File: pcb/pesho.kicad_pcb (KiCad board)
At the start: 2 copper layers, 102.5 x 65 mm, 58 parts, among them IC1 4N25, IC2 4N25, IC3 4N25, IC4 4N25, IC5 4N25, IC6 4N25, P1 Power, P2 Bulkey, P3 Raspberry Pi CONN, P4 Serial, U1 JE-112D, U2 JE-112D, U3 JE-112D

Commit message: added test pcb segment
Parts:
- moved C10 142.8 mm to (238.8, 77.8)
- moved C11 142.8 mm to (238.8, 80.3)
- moved C13 142.8 mm to (238.8, 85.3)
- moved C15 142.8 mm to (238.8, 90.3)
- moved C16 142.8 mm to (238.8, 92.8)
- moved C3 142.8 mm to (238.8, 60.3)
- moved C4 142.8 mm to (238.8, 62.8)
- moved C5 142.8 mm to (238.8, 65.3)
- moved C6 142.8 mm to (238.8, 67.8)
- moved C7 142.8 mm to (238.8, 70.3)
- moved C9 142.8 mm to (238.8, 75.3)
- moved R4 142.8 mm to (244.8, 85.3)
- moved R5 142.8 mm to (244.8, 82.8)
- moved R6 142.8 mm to (244.8, 80.3)
- moved D1 82.1 mm to (204.8, 62.8)
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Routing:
- net Net-(D6-Pad1): track 40.4 -> 111.6 mm, vias 0 -> 1
- net Net-(D5-Pad1): track 22.1 -> 87.7 mm, vias 0 -> 1
- net /BLK: track 0.00 -> 43.1 mm
- net /BD: track 0.00 -> 43.0 mm
- net /BUK: track 0.00 -> 41.4 mm
- net +12V: track 257.6 -> 228.9 mm
- net Net-(D4-Pad1): track 45.5 -> 63.1 mm
- net GNDA: track 50.9 -> 57.1 mm, vias 0 -> 1
- net (no net): vias 0 -> 440
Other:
- board size 102.5 x 65 mm -> 102.5 x 95 mm
- board text added: "Initlab Pesho PCB"
- board text added: "rdrlab"

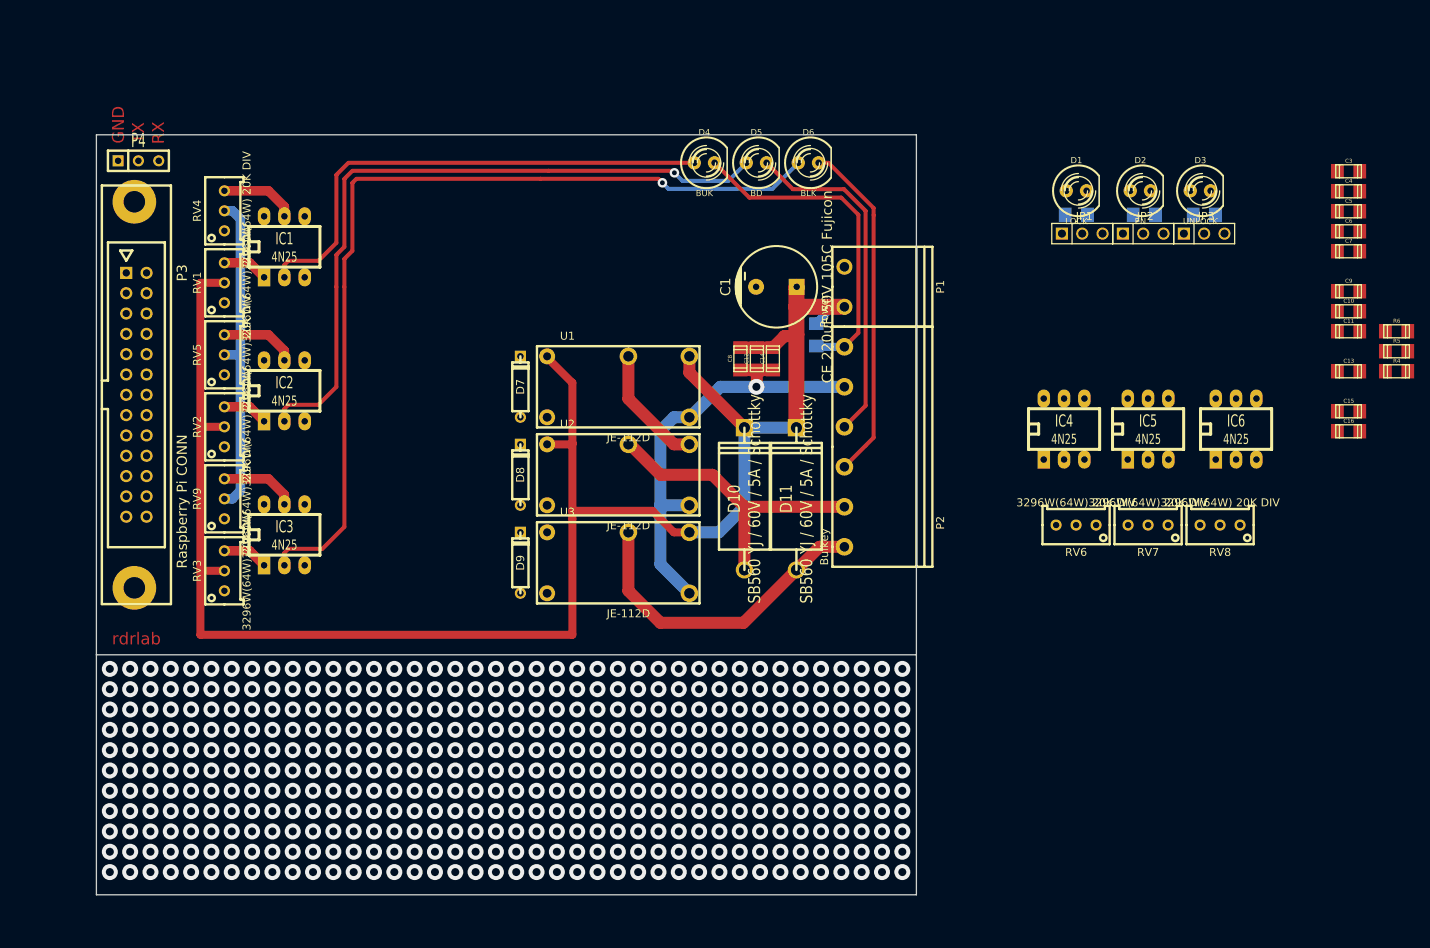
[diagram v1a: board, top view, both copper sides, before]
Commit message: better layout and all components on place
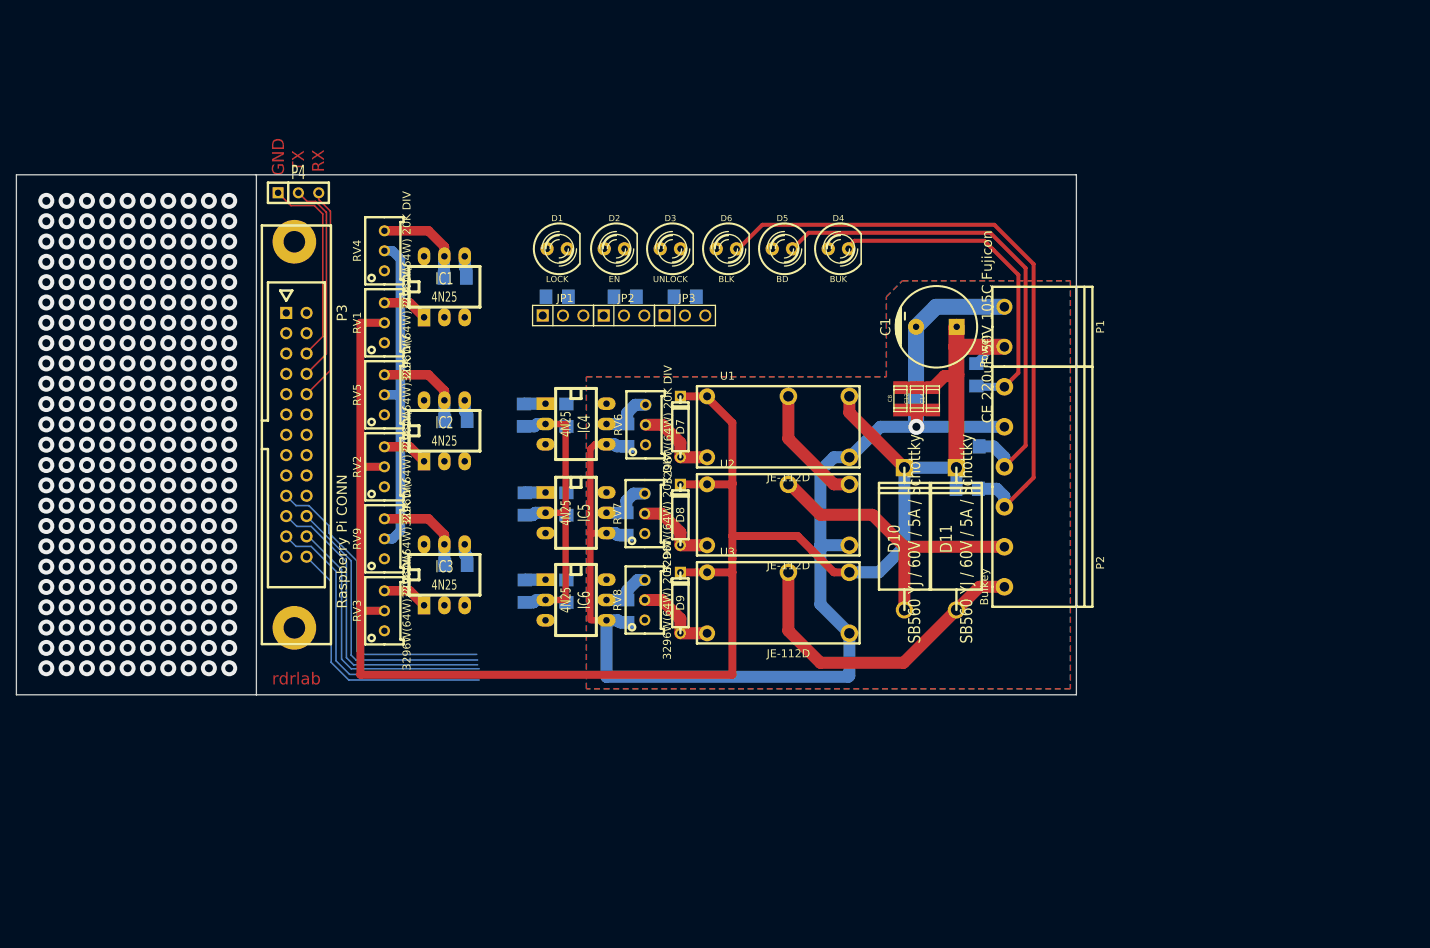
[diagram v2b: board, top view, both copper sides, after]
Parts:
- C10, C11, C13, C15, C16, C3, C4, C5, C6, C7, C9, R4, R5, R6: moved to B.Cu
- moved C16 112.8 mm to (127.2, 109.5), turned to 180 degrees
- moved C13 112.3 mm to (127.1, 73.6), turned to 180 degrees
- moved C15 111.6 mm to (127.2, 91.5), turned to 180 degrees
- moved C7 111.4 mm to (135.8, 112.8), turned to 90 degrees
- moved R6 108.7 mm to (141.0, 112.8), turned to 90 degrees
- moved C6 108.5 mm to (135.8, 101.9), turned to 90 degrees
- moved C5 106.2 mm to (135.7, 90.8), turned to 90 degrees
- moved R5 105.5 mm to (141.0, 101.9), turned to 90 degrees
- moved R4 103.9 mm to (141.0, 90.8), turned to 90 degrees
- moved C11 96.7 mm to (148.6, 115.3), turned to 90 degrees
- moved C10 94.1 mm to (148.5, 104.4), turned to 90 degrees
- moved C9 91.9 mm to (148.6, 93.3), turned to 90 degrees
- moved IC6 85.2 mm to (142.2, 113.9), turned to 270 degrees
- moved RV8 72.5 mm to (150.8, 113.9), turned to 270 degrees
- moved IC5 72.3 mm to (142.2, 103.0), turned to 270 degrees
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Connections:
- C2 pad 2: /BUK -> /BLK
- C4 pad 2: /BLK -> /BUK
- IC1 pad 2: Net-(D4-Pad1) -> Net-(D6-Pad1)
- IC1 pad 6: Net-(IC1-Pad6) -> (no net)
- IC2 pad 6: Net-(IC2-Pad6) -> (no net)
- IC3 pad 2: Net-(D6-Pad1) -> Net-(D4-Pad1)
- IC3 pad 6: Net-(IC3-Pad6) -> (no net)
- IC4 pad 6: Net-(IC4-Pad6) -> (no net)
- IC5 pad 6: Net-(IC5-Pad6) -> (no net)
- IC6 pad 6: Net-(IC6-Pad6) -> (no net)
- P3 pad 11: Net-(P3-Pad11) -> (no net)
- P3 pad 12: Net-(P3-Pad12) -> (no net)
- P3 pad 13: Net-(P3-Pad13) -> (no net)
- P3 pad 15: Net-(P3-Pad15) -> (no net)
- P3 pad 16: Net-(P3-Pad16) -> (no net)
- P3 pad 18: Net-(P3-Pad18) -> (no net)
- P3 pad 2: Net-(P3-Pad2) -> (no net)
- P3 pad 3: Net-(P3-Pad3) -> (no net)
- P3 pad 4: Net-(P3-Pad4) -> (no net)
- P3 pad 5: Net-(P3-Pad5) -> (no net)
- P3 pad 7: Net-(P3-Pad7) -> (no net)
- RV1 pad 3: Net-(RV1-Pad3) -> (no net)
- RV2 pad 3: Net-(RV2-Pad3) -> (no net)
- RV3 pad 3: Net-(RV3-Pad3) -> (no net)
- RV4 pad 3: Net-(RV4-Pad3) -> (no net)
- RV5 pad 3: Net-(RV5-Pad3) -> (no net)
- RV6 pad 3: Net-(RV6-Pad3) -> (no net)
- RV7 pad 3: Net-(RV7-Pad3) -> (no net)
- RV8 pad 3: Net-(RV8-Pad3) -> (no net)
- RV9 pad 3: Net-(RV9-Pad3) -> (no net)
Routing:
- net Net-(D6-Pad1): track 111.6 -> 0.00 mm, vias 1 -> 0
- net GNDA: track 57.1 -> 160.2 mm
- net Net-(D5-Pad1): track 87.7 -> 0.00 mm, vias 1 -> 0
- net GND: track 0.00 -> 71.6 mm
- net Net-(D4-Pad1): track 63.1 -> 0.00 mm
- net /GPIO10: track 0.00 -> 39.2 mm
- net /GPIO9: track 0.00 -> 38.6 mm
- net /GPIO25: track 9.52 -> 48.0 mm
- net /GPIO11: track 0.00 -> 37.8 mm
- net /GPIO8: track 9.52 -> 47.1 mm
- net /GPIO7: track 9.52 -> 46.0 mm
- net /BLK: track 43.1 -> 77.1 mm
- net /RX: track 0.00 -> 27.0 mm
- net /TX: track 0.00 -> 25.7 mm
- net /BD: track 43.0 -> 62.6 mm
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- added copper zone on B.Cu, net GNDA
- added copper zone on F.Cu, net GNDA
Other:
- board size 102.5 x 95 mm -> 132.5 x 65 mm

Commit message: added some traces
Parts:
- R1, R2, R3: moved to F.Cu
- moved R2 1.35 mm to (147.0, 76.0)
- moved R3 1.10 mm to (154.8, 76.0)
- moved R1 0.60 mm to (139.2, 76.0), turned to 0 degrees
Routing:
- net Net-(D4-Pad1): track 0.00 -> 86.2 mm
- net Net-(D5-Pad1): track 0.00 -> 62.1 mm
- net GND: track 71.6 -> 115.2 mm
- net Net-(D6-Pad1): track 0.00 -> 38.4 mm
- net /GPIO25: track 48.0 -> 75.9 mm
- net +3.3V: track 40.8 -> 58.7 mm

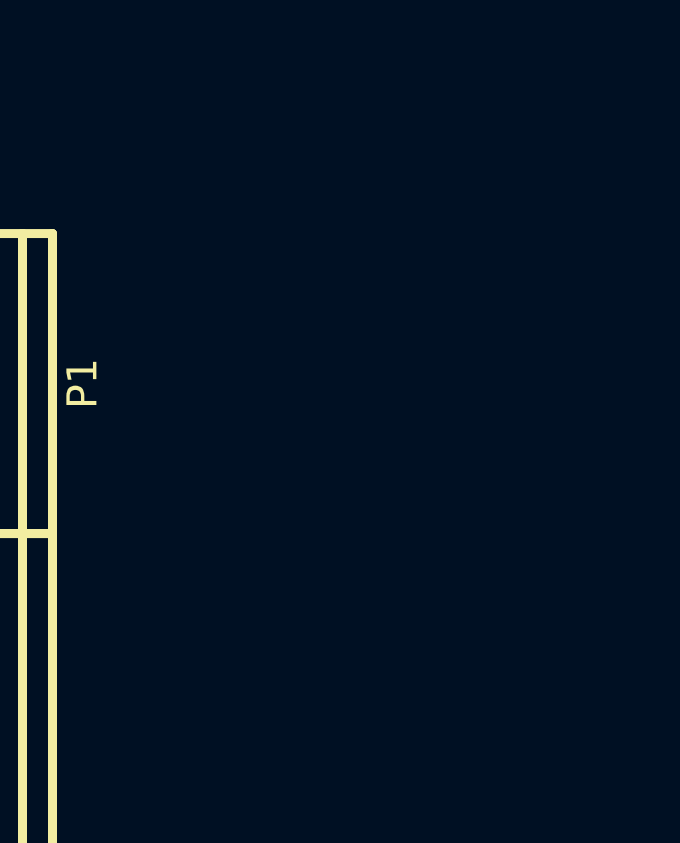
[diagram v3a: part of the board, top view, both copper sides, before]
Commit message: 2 serial diodes added for protection.
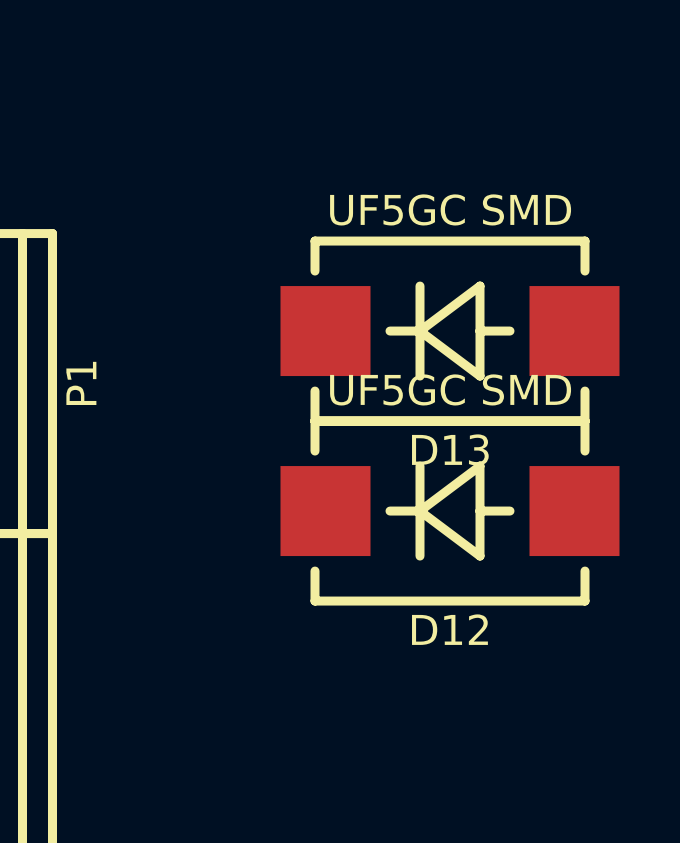
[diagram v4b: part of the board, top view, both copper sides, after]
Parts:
- added D12: UF5GC SMD, pesho:DO-214AB, F.Cu at (220.0, 84.0)
- added D13: UF5GC SMD, pesho:DO-214AB, F.Cu at (220.0, 78.0)
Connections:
- IC1 pad 6: (no net) -> Net-(IC1-Pad6)
- IC2 pad 6: (no net) -> Net-(IC2-Pad6)
- IC3 pad 6: (no net) -> Net-(IC3-Pad6)
- IC4 pad 6: (no net) -> Net-(IC4-Pad6)
- IC5 pad 6: (no net) -> Net-(IC5-Pad6)
- IC6 pad 6: (no net) -> Net-(IC6-Pad6)
- P1 pad 1: +12V -> Net-(D12-Pad1)
- P3 pad 11: (no net) -> Net-(P3-Pad11)
- P3 pad 12: (no net) -> Net-(P3-Pad12)
- P3 pad 13: (no net) -> Net-(P3-Pad13)
- P3 pad 15: (no net) -> Net-(P3-Pad15)
- P3 pad 16: (no net) -> Net-(P3-Pad16)
- P3 pad 18: (no net) -> Net-(P3-Pad18)
- P3 pad 2: (no net) -> Net-(P3-Pad2)
- P3 pad 3: (no net) -> Net-(P3-Pad3)
- P3 pad 4: (no net) -> Net-(P3-Pad4)
- P3 pad 5: (no net) -> Net-(P3-Pad5)
- P3 pad 7: (no net) -> Net-(P3-Pad7)
- RV1 pad 3: (no net) -> Net-(RV1-Pad3)
- RV2 pad 3: (no net) -> Net-(RV2-Pad3)
- RV3 pad 3: (no net) -> Net-(RV3-Pad3)
- RV4 pad 3: (no net) -> Net-(RV4-Pad3)
- RV5 pad 3: (no net) -> Net-(RV5-Pad3)
- RV6 pad 3: (no net) -> Net-(RV6-Pad3)
- RV7 pad 3: (no net) -> Net-(RV7-Pad3)
- RV8 pad 3: (no net) -> Net-(RV8-Pad3)
- RV9 pad 3: (no net) -> Net-(RV9-Pad3)
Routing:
- net Net-(D12-Pad1): track 0.00 -> 7.50 mm
- net +12V: track 248.3 -> 240.8 mm

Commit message: Final version of the pcb.
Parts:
- moved D13 37.1 mm to (183.0, 80.0), turned to 270 degrees
- moved D12 31.3 mm to (189.0, 80.0), turned to 270 degrees
- moved C4 14.8 mm to (191.8, 85.2)
- moved C2 14.3 mm to (191.2, 100.0), turned to 180 degrees
- moved C1 12.8 mm to (174.5, 79.8), turned to 0 degrees
- moved R5 5.52 mm to (137.0, 98.1), turned to 0 degrees
- moved R4 5.52 mm to (137.0, 87.0), turned to 0 degrees
- moved R6 5.16 mm to (137.2, 109.2), turned to 0 degrees
- moved R1 2.75 mm to (142.0, 76.0)
- moved R2 2.50 mm to (149.5, 76.0), turned to 180 degrees
- moved R3 2.50 mm to (157.2, 76.0), turned to 180 degrees
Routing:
- net GND: track 115.2 -> 212.8 mm, vias 0 -> 22
- net /GPIO11: track 37.8 -> 133.2 mm, vias 0 -> 1
- net /GPIO9: track 38.6 -> 131.9 mm, vias 0 -> 1
- net /GPIO10: track 39.2 -> 127.7 mm, vias 0 -> 1
- net +3.3V: track 58.7 -> 81.9 mm
- net /GPIO7: track 46.0 -> 23.8 mm, vias 0 -> 1
- net /GPIO25: track 75.9 -> 55.7 mm
- net GNDA: track 160.2 -> 172.9 mm, vias 1 -> 5
- net Net-(D12-Pad1): track 7.50 -> 16.6 mm
- net Net-(D3-Pad2): track 0.00 -> 7.40 mm
- net Net-(D2-Pad2): track 0.00 -> 7.09 mm
- net Net-(D1-Pad2): track 0.00 -> 6.94 mm
- net /GPIO8: track 47.1 -> 41.0 mm, vias 0 -> 1
- net +12V: track 240.8 -> 246.7 mm, vias 0 -> 1
- net Net-(JP2-Pad2): track 0.00 -> 2.52 mm
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- added copper zone on B.Cu, net GND
- added copper zone on F.Cu, net GND
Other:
- board text added: "LOCK | EN | UNLOCK | BLK | BD | BUK"

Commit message: Latest layout submitted to bulged for films.
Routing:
- net GND: track 212.8 -> 212.5 mm, vias 22 -> 0
- net GNDA: vias 5 -> 2
- net (no net): vias 240 -> 242
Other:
- board text added: "PESHO rev.A"

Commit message: Last version with fixed drills and send for production.
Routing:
- net GNDA: vias 2 -> 3

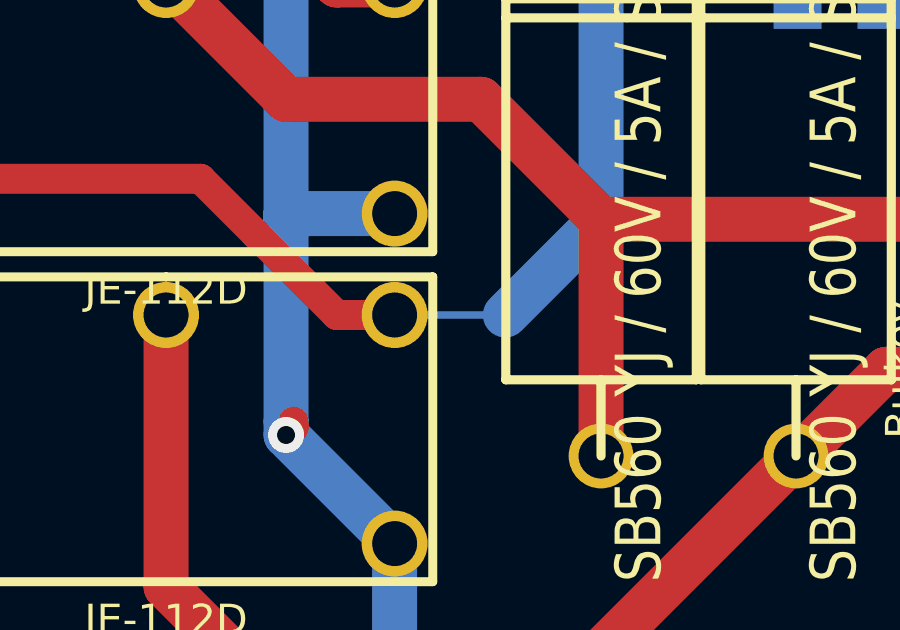
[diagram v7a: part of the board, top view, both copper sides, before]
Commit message: Fixed small bug in the pcb on one of the Relays.
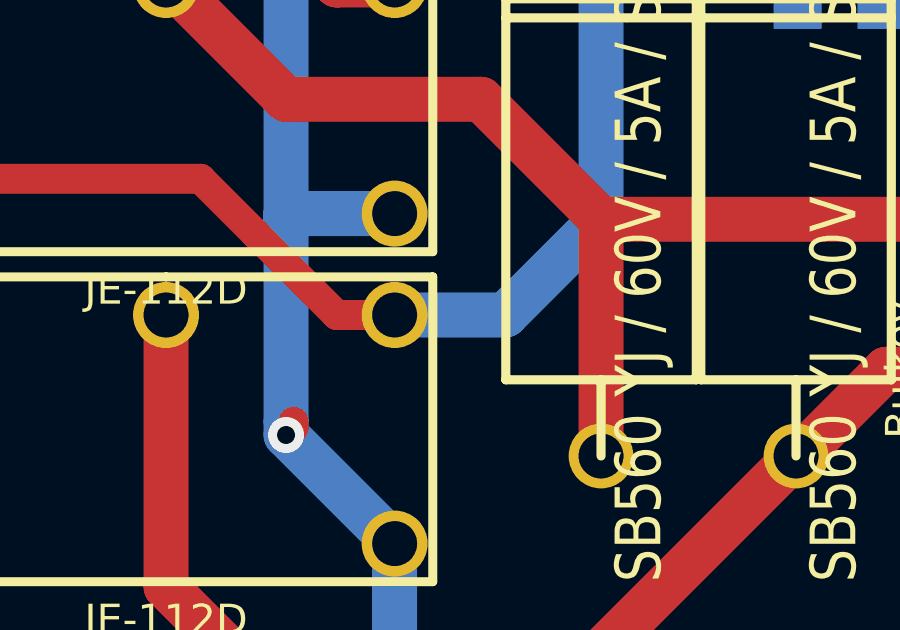
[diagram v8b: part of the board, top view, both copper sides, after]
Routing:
- net GNDA: vias 3 -> 2
- net (no net): vias 242 -> 243
